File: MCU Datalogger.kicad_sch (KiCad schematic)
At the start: 25 parts, among them U1 24LC1025, U2 24LC1025, U3 DS1337S_, U4 ATMEGA328P-AU, Y1 Crystal, Y2 Crystal

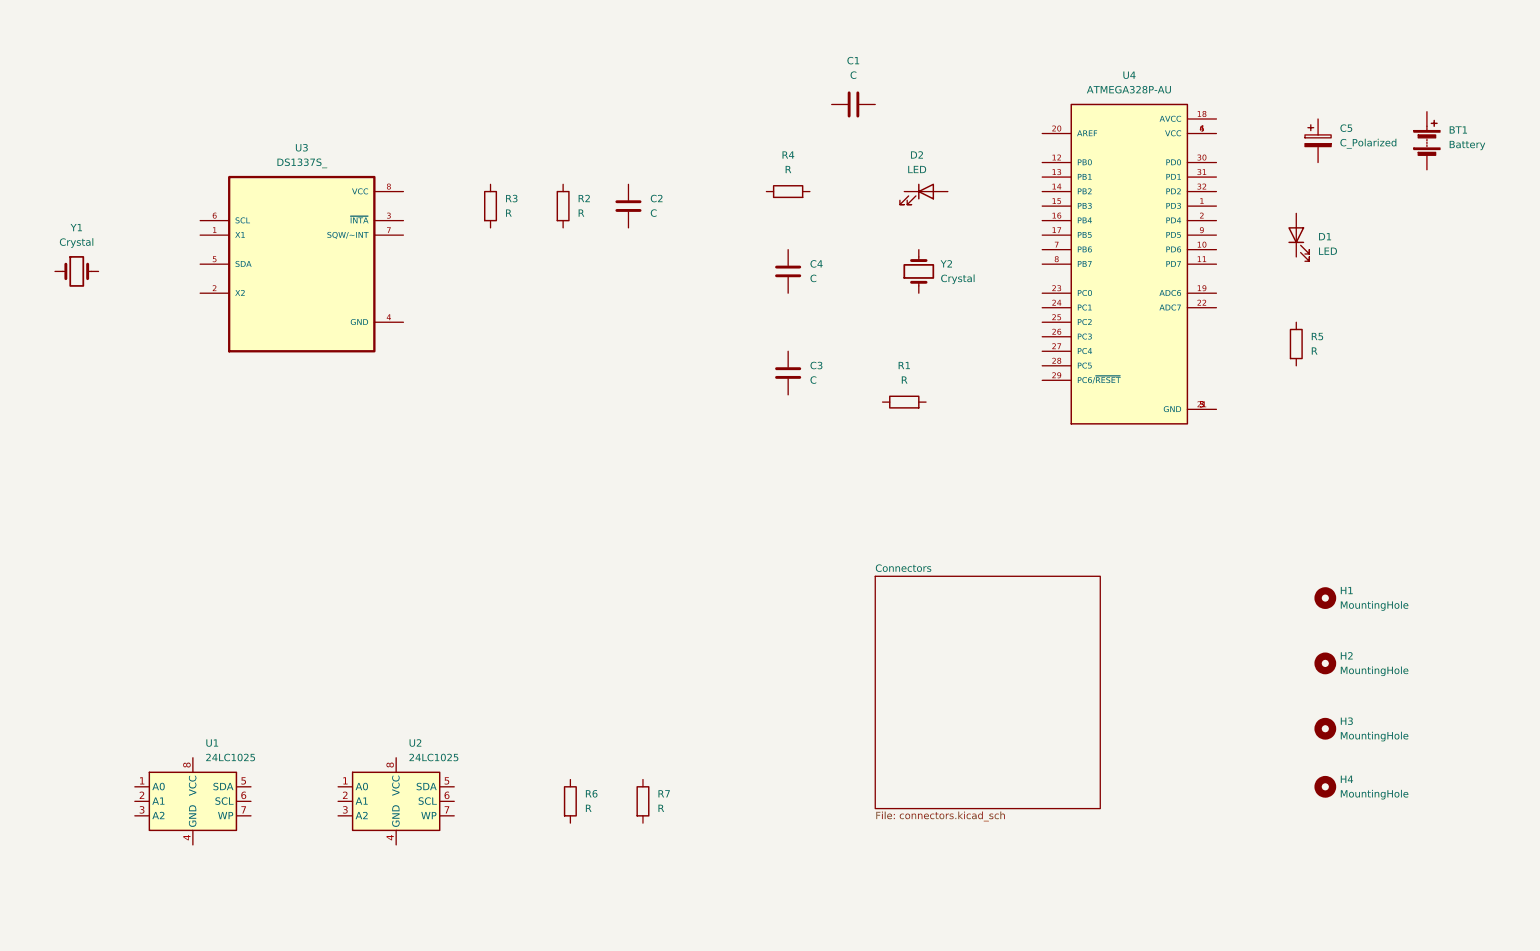
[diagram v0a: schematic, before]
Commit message: Added component values.
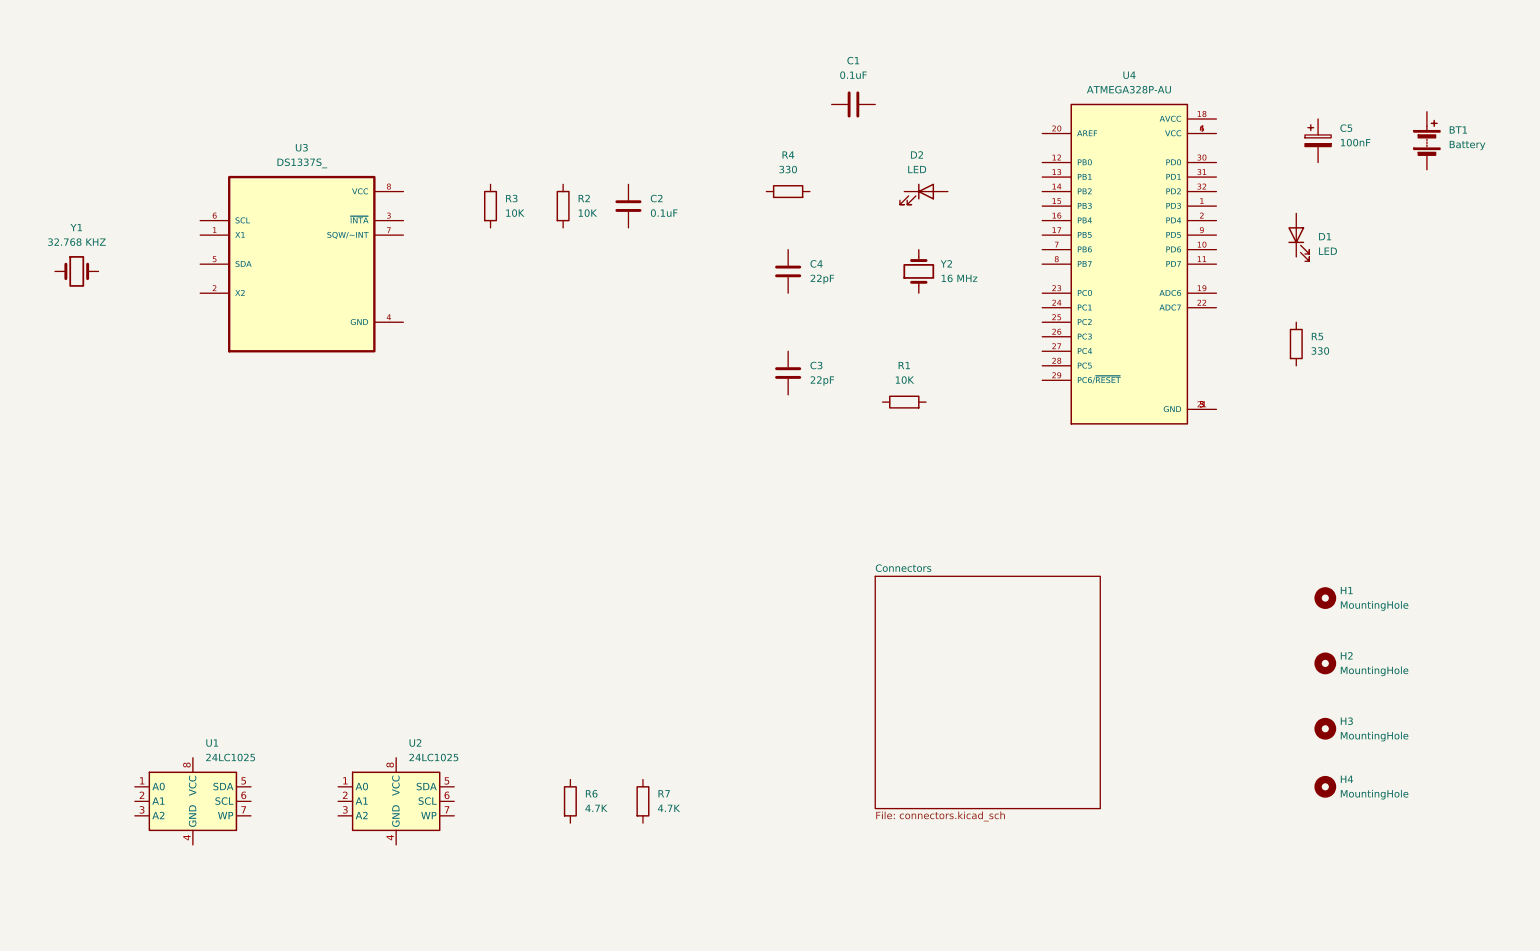
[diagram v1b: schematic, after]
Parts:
- C1, C2: value C -> 0.1uF
- C3, C4: value C -> 22pF
- C5: value C_Polarized -> 100nF
- R1, R2, R3: value R -> 10K
- R4, R5: value R -> 330
- R6, R7: value R -> 4.7K
- Y1: value Crystal -> 32.768 KHZ
- Y2: value Crystal -> 16 MHz
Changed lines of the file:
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@@
       (effects (font (size 1.27 1.27)) (justify left))
     )
-    (property "Value" "R" (at 243.84 73.66 0)
+    (property "Value" "330" (at 243.84 73.66 0)
       (effects (font (size 1.27 1.27)) (justify left))
     )
@@
     (property "Datasheet" "~" (at 241.3 72.39 0)
       (effects (font (size 1.27 1.27)) hide)
+    )
+    (property "Purpose" "" (at 241.3 72.39 0)
+      (effects (font (size 1.27 1.27)))
     )
     (pin "1")
@@
       (effects (font (size 1.27 1.27)) (justify left))
     )
-    (property "Value" "R" (at 115.57 49.53 0)
+    (property "Value" "10K" (at 115.57 49.53 0)
       (effects (font (size 1.27 1.27)) (justify left))
     )
@@
       (effects (font (size 1.27 1.27)) hide)
     )
+    (property "Purpose" "" (at 113.03 48.26 0)
+      (effects (font (size 1.27 1.27)))
+    )
     (pin "1")
     (pin "2")
@@
       (effects (font (size 1.27 1.27)) (justify left))
     )
-    (property "Value" "R" (at 129.54 153.67 0)
+    (property "Value" "4.7K" (at 129.54 153.67 0)
       (effects (font (size 1.27 1.27)) (justify left))
     )
@@
       (effects (font (size 1.27 1.27)) hide)
     )
+    (property "Purpose" "" (at 127 152.4 0)
+      (effects (font (size 1.27 1.27)))
+    )
     (pin "1")
     (pin "2")
@@
       (effects (font (size 1.27 1.27)))
     )
-    (property "Value" "Crystal" (at 27.94 54.61 0)
+    (property "Value" "32.768 KHZ" (at 27.94 54.61 0)
       (effects (font (size 1.27 1.27)))
     )
@@
       (effects (font (size 1.27 1.27)) hide)
     )
+    (property "Purpose" "" (at 27.94 59.69 0)
+      (effects (font (size 1.27 1.27)))
+    )
     (pin "2")
     (pin "1")
@@
       (effects (font (size 1.27 1.27)) (justify left))
     )
-    (property "Value" "C" (at 128.27 49.53 0)
+    (property "Value" "0.1uF" (at 128.27 49.53 0)
       (effects (font (size 1.27 1.27)) (justify left))
     )
@@
       (effects (font (size 1.27 1.27)) hide)
     )
+    (property "Purpose" "" (at 124.46 48.26 0)
+      (effects (font (size 1.27 1.27)))
+    )
     (pin "1")
     (pin "2")
@@
       (effects (font (size 1.27 1.27)))
     )
-    (property "Value" "R" (at 172.72 78.74 90)
+    (property "Value" "10K" (at 172.72 78.74 90)
       (effects (font (size 1.27 1.27)))
     )
@@
     (property "Datasheet" "~" (at 172.72 82.55 0)
       (effects (font (size 1.27 1.27)) hide)
+    )
+    (property "Purpose" "" (at 172.72 82.55 0)
+      (effects (font (size 1.27 1.27)))
     )
     (pin "1")
@@
       (effects (font (size 1.27 1.27)))
     )
-    (property "Value" "C" (at 163.83 25.4 90)
+    (property "Value" "0.1uF" (at 163.83 25.4 90)
       (effects (font (size 1.27 1.27)))
     )
@@
       (effects (font (size 1.27 1.27)) hide)
     )
+    (property "Purpose" "" (at 163.83 30.48 0)
+      (effects (font (size 1.27 1.27)))
+    )
     (pin "1")
     (pin "2")
@@
       (effects (font (size 1.27 1.27)) (justify left))
     )
-    (property "Value" "R" (at 102.87 49.53 0)
+    (property "Value" "10K" (at 102.87 49.53 0)
       (effects (font (size 1.27 1.27)) (justify left))
     )
@@
       (effects (font (size 1.27 1.27)) hide)
     )
+    (property "Purpose" "" (at 100.33 48.26 0)
+      (effects (font (size 1.27 1.27)))
+    )
     (pin "1")
     (pin "2")
@@
       (effects (font (size 1.27 1.27)))
     )
-    (property "Value" "R" (at 152.4 41.91 90)
+    (property "Value" "330" (at 152.4 41.91 90)
       (effects (font (size 1.27 1.27)))
     )
@@
     (property "Datasheet" "~" (at 152.4 45.72 0)
       (effects (font (size 1.27 1.27)) hide)
+    )
+    (property "Purpose" "" (at 152.4 45.72 0)
+      (effects (font (size 1.27 1.27)))
     )
     (pin "1")
@@
       (effects (font (size 1.27 1.27)) (justify left))
     )
-    (property "Value" "C_Polarized" (at 248.92 37.211 0)
+    (property "Value" "100nF" (at 248.92 37.211 0)
       (effects (font (size 1.27 1.27)) (justify left))
     )
@@
       (effects (font (size 1.27 1.27)) hide)
     )
+    (property "Purpose" "" (at 245.11 36.83 0)
+      (effects (font (size 1.27 1.27)))
+    )
     (pin "1")
     (pin "2")
@@
       (effects (font (size 1.27 1.27)) (justify left))
     )
-    (property "Value" "C" (at 156.21 60.96 0)
+    (property "Value" "22pF" (at 156.21 60.96 0)
       (effects (font (size 1.27 1.27)) (justify left))
     )
@@
     (property "Datasheet" "~" (at 152.4 59.69 0)
       (effects (font (size 1.27 1.27)) hide)
+    )
+    (property "Purpose" "" (at 152.4 59.69 0)
+      (effects (font (size 1.27 1.27)))
     )
     (pin "1")
@@
       (effects (font (size 1.27 1.27)) (justify right))
     )
-    (property "Value" "Crystal" (at 179.07 60.96 90)
+    (property "Value" "16 MHz" (at 179.07 60.96 90)
       (effects (font (size 1.27 1.27)) (justify right))
     )
@@
     (property "Datasheet" "~" (at 175.26 59.69 0)
       (effects (font (size 1.27 1.27)) hide)
+    )
+    (property "Purpose" "" (at 175.26 59.69 0)
+      (effects (font (size 1.27 1.27)))
     )
     (pin "2")
@@
       (effects (font (size 1.27 1.27)) (justify left))
     )
-    (property "Value" "C" (at 156.21 78.74 0)
+    (property "Value" "22pF" (at 156.21 78.74 0)
       (effects (font (size 1.27 1.27)) (justify left))
     )
@@
       (effects (font (size 1.27 1.27)) hide)
     )
+    (property "Purpose" "" (at 152.4 77.47 0)
+      (effects (font (size 1.27 1.27)))
+    )
     (pin "1")
     (pin "2")
@@
       (effects (font (size 1.27 1.27)) (justify left))
     )
-    (property "Value" "R" (at 116.84 153.67 0)
+    (property "Value" "4.7K" (at 116.84 153.67 0)
       (effects (font (size 1.27 1.27)) (justify left))
     )
@@
       (effects (font (size 1.27 1.27)) hide)
     )
-    (pin "1")
+    (property "Purpose" "" (at 114.3 152.4 0)
+      (effects (font (size 1.27 1.27)))
+    )
+    (pin "1")

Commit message: Completed symbol-footprint associations.
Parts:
- BT1: footprint (none) -> Connector_PinHeader_2.54mm:PinHeader_1x02_P2.54mm_Vertical
- C1, C2, C3, C4, C5: footprint (none) -> Capacitor_SMD:C_0805_2012Metric
- D1, D2: footprint (none) -> LED_SMD:LED_0805_2012Metric
- H1, H2, H3, H4: footprint (none) -> MountingHole:MountingHole_2.1mm
- R1, R2, R3, R4, R5, R6, R7: footprint (none) -> Resistor_SMD:R_0805_2012Metric
- U1, U2: footprint (none) -> Package_SO:SOIC-8_5.23x5.23mm_P1.27mm
- U3: footprint DS1337S_:SOIC127P600X175-8N -> Footprints:SOIC127P600X175-8N
- U4: footprint ATMEGA328P-AU:QFP80P900X900X120-32N -> Footprints:QFP80P900X900X120-32N
- Y1, Y2: footprint (none) -> Crystal:Crystal_SMD_5032-2Pin_5.0x3.2mm_HandSoldering
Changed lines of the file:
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@@
       (effects (font (size 1.27 1.27)) (justify left))
     )
-    (property "Footprint" "" (at 239.522 72.39 90)
+    (property "Footprint" "Resistor_SMD:R_0805_2012Metric" (at 239.522 72.39 90)
       (effects (font (size 1.27 1.27)) hide)
     )
@@
       (effects (font (size 1.27 1.27)) (justify left))
     )
-    (property "Footprint" "" (at 83.82 152.4 0)
+    (property "Footprint" "Package_SO:SOIC-8_5.23x5.23mm_P1.27mm" (at 83.82 152.4 0)
       (effects (font (size 1.27 1.27)) hide)
     )
@@
       (effects (font (size 1.27 1.27)) (justify left))
     )
-    (property "Footprint" "" (at 111.252 48.26 90)
+    (property "Footprint" "Resistor_SMD:R_0805_2012Metric" (at 111.252 48.26 90)
       (effects (font (size 1.27 1.27)) hide)
     )
@@
       (effects (font (size 1.27 1.27)) (justify left))
     )
-    (property "Footprint" "" (at 246.38 139.7 0)
+    (property "Footprint" "MountingHole:MountingHole_2.1mm" (at 246.38 139.7 0)
       (effects (font (size 1.27 1.27)) hide)
     )
@@
       (effects (font (size 1.27 1.27)) (justify left))
     )
-    (property "Footprint" "" (at 125.222 152.4 90)
+    (property "Footprint" "Resistor_SMD:R_0805_2012Metric" (at 125.222 152.4 90)
       (effects (font (size 1.27 1.27)) hide)
     )
@@
       (effects (font (size 1.27 1.27)))
     )
-    (property "Footprint" "" (at 27.94 59.69 0)
+    (property "Footprint" "Crystal:Crystal_SMD_5032-2Pin_5.0x3.2mm_HandSoldering" (at 27.94 59.69 0)
       (effects (font (size 1.27 1.27)) hide)
     )
@@
       (effects (font (size 1.27 1.27)) (justify left))
     )
-    (property "Footprint" "" (at 246.38 149.86 0)
+    (property "Footprint" "MountingHole:MountingHole_2.1mm" (at 246.38 149.86 0)
       (effects (font (size 1.27 1.27)) hide)
     )
@@
       (effects (font (size 1.27 1.27)) (justify left))
     )
-    (property "Footprint" "" (at 246.38 116.84 0)
+    (property "Footprint" "MountingHole:MountingHole_2.1mm" (at 246.38 116.84 0)
       (effects (font (size 1.27 1.27)) hide)
     )
@@
       (effects (font (size 1.27 1.27)) (justify left))
     )
-    (property "Footprint" "" (at 264.16 35.306 90)
+    (property "Footprint" "Connector_PinHeader_2.54mm:PinHeader_1x02_P2.54mm_Vertical" (at 264.16 35.306 90)
       (effects (font (size 1.27 1.27)) hide)
     )
@@
       (effects (font (size 1.27 1.27)) (justify left))
     )
-    (property "Footprint" "" (at 125.4252 52.07 0)
+    (property "Footprint" "Capacitor_SMD:C_0805_2012Metric" (at 125.4252 52.07 0)
       (effects (font (size 1.27 1.27)) hide)
     )
@@
       (effects (font (size 1.27 1.27)))
     )
-    (property "Footprint" "" (at 172.72 84.328 90)
+    (property "Footprint" "Resistor_SMD:R_0805_2012Metric" (at 172.72 84.328 90)
       (effects (font (size 1.27 1.27)) hide)
     )
@@
       (effects (font (size 1.27 1.27)))
     )
-    (property "Footprint" "" (at 176.53 45.72 0)
+    (property "Footprint" "LED_SMD:LED_0805_2012Metric" (at 176.53 45.72 0)
       (effects (font (size 1.27 1.27)) hide)
     )
@@
       (effects (font (size 1.27 1.27)))
     )
-    (property "Footprint" "" (at 167.64 29.5148 0)
+    (property "Footprint" "Capacitor_SMD:C_0805_2012Metric" (at 167.64 29.5148 0)
       (effects (font (size 1.27 1.27)) hide)
     )
@@
       (effects (font (size 1.27 1.27)) (justify left))
     )
-    (property "Footprint" "" (at 98.552 48.26 90)
+    (property "Footprint" "Resistor_SMD:R_0805_2012Metric" (at 98.552 48.26 90)
       (effects (font (size 1.27 1.27)) hide)
     )
@@
       (effects (font (size 1.27 1.27)))
     )
-    (property "Footprint" "" (at 152.4 47.498 90)
+    (property "Footprint" "Resistor_SMD:R_0805_2012Metric" (at 152.4 47.498 90)
       (effects (font (size 1.27 1.27)) hide)
     )
@@
       (effects (font (size 1.27 1.27)))
     )
-    (property "Footprint" "ATMEGA328P-AU:QFP80P900X900X120-32N" (at 212.09 58.42 0)
+    (property "Footprint" "Footprints:QFP80P900X900X120-32N" (at 212.09 58.42 0)
       (effects (font (size 1.27 1.27)) (justify bottom) hide)
     )
@@
       (effects (font (size 1.27 1.27)) (justify left))
     )
-    (property "Footprint" "" (at 246.0752 40.64 0)
+    (property "Footprint" "Capacitor_SMD:C_0805_2012Metric" (at 246.0752 40.64 0)
       (effects (font (size 1.27 1.27)) hide)
     )
@@
       (effects (font (size 1.27 1.27)) (justify left))
     )
-    (property "Footprint" "" (at 153.3652 63.5 0)
+    (property "Footprint" "Capacitor_SMD:C_0805_2012Metric" (at 153.3652 63.5 0)
       (effects (font (size 1.27 1.27)) hide)
     )
@@
       (effects (font (size 1.27 1.27)) (justify right))
     )
-    (property "Footprint" "" (at 175.26 59.69 0)
+    (property "Footprint" "Crystal:Crystal_SMD_5032-2Pin_5.0x3.2mm_HandSoldering" (at 175.26 59.69 0)
       (effects (font (size 1.27 1.27)) hide)
     )
@@
       (effects (font (size 1.27 1.27)) (justify left))
     )
-    (property "Footprint" "" (at 48.26 152.4 0)
+    (property "Footprint" "Package_SO:SOIC-8_5.23x5.23mm_P1.27mm" (at 48.26 152.4 0)
       (effects (font (size 1.27 1.27)) hide)
     )
@@
       (effects (font (size 1.27 1.27)))
     )
-    (property "Footprint" "DS1337S_:SOIC127P600X175-8N" (at 67.31 58.42 0)
+    (property "Footprint" "Footprints:SOIC127P600X175-8N" (at 67.31 58.42 0)
       (effects (font (size 1.27 1.27)) (justify bottom) hide)
     )
@@
       (effects (font (size 1.27 1.27)) (justify right))
     )
-    (property "Footprint" "" (at 241.3 53.34 0)
+    (property "Footprint" "LED_SMD:LED_0805_2012Metric" (at 241.3 53.34 0)
       (effects (font (size 1.27 1.27)) hide)
     )
@@
       (effects (font (size 1.27 1.27)) (justify left))
     )
-    (property "Footprint" "" (at 246.38 128.27 0)
+    (property "Footprint" "MountingHole:MountingHole_2.1mm" (at 246.38 128.27 0)
       (effects (font (size 1.27 1.27)) hide)
     )
@@
       (effects (font (size 1.27 1.27)) (justify left))
     )
-    (property "Footprint" "" (at 153.3652 81.28 0)
+    (property "Footprint" "Capacitor_SMD:C_0805_2012Metric" (at 153.3652 81.28 0)
       (effects (font (size 1.27 1.27)) hide)
     )
@@
       (effects (font (size 1.27 1.27)) (justify left))
     )
-    (property "Footprint" "" (at 112.522 152.4 90)
+    (property "Footprint" "Resistor_SMD:R_0805_2012Metric" (at 112.522 152.4 90)
       (effects (font (size 1.27 1.27)) hide)
     )
@@
   )
   (sheet (at 167.64 113.03) (size 39.37 40.64) (fields_autoplaced)
-    (stroke (width 0.0006) (type solid))
+    (stroke (width 0.0005) (type solid))
     (fill (color 0 0 0 0.0000))
     (property "Sheetname" "Connectors" (at 167.64 112.3943 0)
